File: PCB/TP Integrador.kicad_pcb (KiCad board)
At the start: 2 copper layers, 28 parts, among them Q1 BC547C, Q10 BC547C, Q2 2N3019, Q3 D45H11, Q4 BC547C, Q5 BC557C, Q6 BC557C, Q7 BC547C, Q8 BC557C, Q9 BC547C

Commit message: Upate PCB
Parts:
- added C1: C, Capacitor_THT:CP_Radial_D4.0mm_P1.50mm, F.Cu at (167.6, 86.4)
- added Q11: BC547C, Package_TO_SOT_THT:TO-92_Inline_Wide, F.Cu at (160.0, 73.7)
- added RL2: 50, Resistor_THT:R_Axial_DIN0207_L6.3mm_D2.5mm_P7.62mm_Horizontal, F.Cu at (165.1, 59.7)
- added RL3: 50, Resistor_THT:R_Axial_DIN0207_L6.3mm_D2.5mm_P5.08mm_Vertical, F.Cu at (163.0, 77.6)
- added RL4: 50, Resistor_THT:R_Axial_DIN0207_L6.3mm_D2.5mm_P5.08mm_Vertical, F.Cu at (167.6, 81.3)
- moved H3 2.54 mm to (165.1, 106.7)
- moved H4 2.54 mm to (165.1, 43.2)
- moved RD1 2.54 mm to (160.0, 83.8)
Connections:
- Q2 pad 3: vo -> Net-(Q2-E)
- Q3 pad 1: vo -> Net-(Q2-E)
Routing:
- net Net-(Q2-E): track 0.00 -> 41.1 mm
- net GND: track 17.7 -> 8.30 mm
- net Net-(Q11-B): track 0.00 -> 7.96 mm
- net Net-(JP1-B): track 13.5 -> 7.19 mm
- net Net-(Q11-C): track 36.5 -> 42.7 mm
- net vo: track 37.9 -> 31.8 mm

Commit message: Update checkpoint 2
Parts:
- removed C1: C, Capacitor_THT:CP_Radial_D4.0mm_P1.50mm
- removed Q7: BC547C, Package_TO_SOT_THT:TO-92_Inline_Wide
- removed Q8: BC557C, Package_TO_SOT_THT:TO-92_Inline_Wide
- removed RB1: 51, Resistor_THT:R_Axial_DIN0207_L6.3mm_D2.5mm_P7.62mm_Horizontal
- removed RB2: 1.8k, Resistor_THT:R_Axial_DIN0207_L6.3mm_D2.5mm_P7.62mm_Horizontal
- removed RL2: 50, Resistor_THT:R_Axial_DIN0207_L6.3mm_D2.5mm_P7.62mm_Horizontal
- removed RL3, RL4: 50, Resistor_THT:R_Axial_DIN0207_L6.3mm_D2.5mm_P5.08mm_Vertical
- removed VREF1: 1.56, TerminalBlock_Phoenix:TerminalBlock_Phoenix_MKDS-1,5-2-5.08_1x02_P5.08mm_Horizontal
- added CComp1: 12n, Capacitor_THT:CP_Radial_D4.0mm_P1.50mm, F.Cu at (145.2, 74.2)
- added CL1: 2.2u, Capacitor_THT:CP_Radial_D4.0mm_P1.50mm, F.Cu at (183.5, 72.3)
- added JP3: Jumper_2_Bridged, TestPoint:TestPoint_2Pads_Pitch5.08mm_Drill1.3mm, F.Cu at (159.1, 51.4)
- added JP4: Jumper_2_Bridged, TestPoint:TestPoint_2Pads_Pitch5.08mm_Drill1.3mm, F.Cu at (189.5, 53.6)
- added R8: 2200, Resistor_THT:R_Axial_DIN0207_L6.3mm_D2.5mm_P7.62mm_Horizontal, F.Cu at (91.8, 58.2)
- added RP1: 50, Resistor_THT:R_Axial_DIN0207_L6.3mm_D2.5mm_P5.08mm_Vertical, F.Cu at (164.2, 60.3)
- added RP2: 50, Resistor_THT:R_Axial_DIN0207_L6.3mm_D2.5mm_P5.08mm_Vertical, F.Cu at (164.2, 69.1)
- added RS1: 2.2, Resistor_THT:R_Axial_DIN0207_L6.3mm_D2.5mm_P7.62mm_Horizontal, F.Cu at (168.4, 51.6)
- added U1: TL431D, Package_TO_SOT_THT:TO-92_Inline_Wide, F.Cu at (92.3, 75.4)
- Q2: value 2N3019 -> 2SB631; footprint Package_TO_SOT_THT:TO-39-3 -> Package_TO_SOT_THT:TO-126-3_Vertical
- Q3: value D45H11 -> BC547; footprint Package_TO_SOT_THT:TO-220-3_Vertical -> Package_TO_SOT_THT:TO-92_Inline_Wide
- RD1: value 2.2k -> 1k
- moved H3 67.1 mm to (188.2, 43.7)
- moved H2 64.5 mm to (80.1, 42.5)
- moved H4 59.7 mm to (190.1, 97.3)
- moved H1 53.4 mm to (81.6, 96.3)
- moved RL1 33.1 mm to (189.4, 72.4)
- moved JP2 26.8 mm to (135.4, 51.1)
- moved Q9 26.6 mm to (129.1, 86.5)
- moved Q10 21.1 mm to (109.9, 86.2)
- moved JP1 20.4 mm to (158.8, 79.4)
- moved RD1 19.7 mm to (175.7, 71.9), turned to -90 degrees
- moved RD2 17.0 mm to (168.9, 83.5), turned to 180 degrees
- moved Q11 16.8 mm to (175.4, 66.8), turned to 90 degrees
- moved Q3 16.0 mm to (146.3, 62.2), turned to 0 degrees
- moved R2 14.8 mm to (103.3, 91.2), turned to 180 degrees
- moved RE1 14.5 mm to (122.0, 91.3), turned to -90 degrees
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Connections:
- net vref renamed Net-(Q1-B)
- JP2 pad 1: Net-(JP2-A) -> vi
- Q1 pad 1: Net-(JP2-A) -> Net-(Q1-C)
- Q11 pad 3: vo -> Net-(JP4-A)
- Q2 pad 1: Net-(Q2-C) -> Net-(JP2-B)
- Q2 pad 2: Net-(Q11-C) -> Net-(JP3-A)
- Q3 pad 2: Net-(Q2-C) -> Net-(Q11-C)
- Q3 pad 3: vi -> Net-(JP3-A)
- Q4 pad 1: Net-(Q4-C) -> Net-(Q11-C)
- Q5 pad 1: Net-(Q4-C) -> Net-(Q11-C)
- Q5 pad 2: Net-(Q4-C) -> Net-(Q1-C)
- Q6 pad 1: Net-(JP2-A) -> Net-(Q1-C)
- Q6 pad 2: Net-(Q4-C) -> Net-(Q1-C)
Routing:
- net GND: track 8.30 -> 212.7 mm
- net Net-(Q4-C): track 50.0 -> 0.00 mm
- net Net-(Q10-B): track 64.2 -> 26.1 mm
- net Net-(Q1-C): track 0.00 -> 37.5 mm
- net Net-(Q2-B): track 41.1 -> 5.98 mm
- net Net-(JP2-A): track 32.2 -> 0.00 mm
- net Net-(Q11-C): track 42.7 -> 74.4 mm
- net Net-(JP4-A): track 0.00 -> 24.7 mm
- net Net-(JP3-A): track 0.00 -> 21.3 mm
- net Net-(JP1-A): track 13.5 -> 29.9 mm
- net Net-(Q8-E): track 15.6 -> 0.00 mm
- net Net-(Q2-C): track 13.8 -> 0.00 mm
- net Net-(JP3-B): track 0.00 -> 8.26 mm
- net Net-(JP1-B): track 7.19 -> 15.2 mm
- net Net-(Q11-B): track 7.96 -> 14.9 mm
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- removed copper zone on B.Cu, net GND

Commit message: Edit Checkpoint 2
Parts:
- added JP5: Jumper_2_Bridged, TestPoint:TestPoint_2Pads_Pitch5.08mm_Drill1.3mm, F.Cu at (117.7, 82.0)
- added JP6: Jumper_2_Bridged, TestPoint:TestPoint_2Pads_Pitch5.08mm_Drill1.3mm, F.Cu at (134.4, 73.5)
- added JP7: Jumper_2_Bridged, TestPoint:TestPoint_2Pads_Pitch5.08mm_Drill1.3mm, F.Cu at (170.6, 63.6)
- added JP8: Jumper_2_Bridged, TestPoint:TestPoint_2Pads_Pitch5.08mm_Drill1.3mm, F.Cu at (93.6, 75.8)
- CComp1, CL1: footprint Capacitor_THT:CP_Radial_D4.0mm_P1.50mm -> Capacitor_THT:CP_Radial_D8.0mm_P3.80mm
- moved Q11 7.13 mm to (182.5, 66.3)
- moved CL1 5.07 mm to (180.9, 76.6)
- moved U1 3.96 mm to (88.3, 75.4)
- moved VI1 3.76 mm to (83.7, 50.8)
- moved H2 3.56 mm to (83.6, 42.5)
- moved RD1 3.37 mm to (172.4, 72.2)
- moved H1 2.30 mm to (83.6, 97.4)
- moved H4 1.52 mm to (188.6, 97.4)
- moved H3 1.33 mm to (188.6, 42.5)
- moved CComp1 1.17 mm to (144.4, 73.3), turned to 0 degrees
- moved Q2 0.11 mm to (146.6, 51.2)
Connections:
- CComp1 pad 1: Net-(Q11-C) -> Net-(JP6-B)
- Q1 pad 2: Net-(Q1-B) -> Net-(JP8-B)
- Q1 pad 3: Net-(Q1-E) -> Net-(JP5-A)
- Q11 pad 1: Net-(Q11-C) -> Net-(JP6-B)
- Q11 pad 2: Net-(Q11-B) -> Net-(JP7-B)
- Q3 pad 2: Net-(Q11-C) -> Net-(JP6-B)
- Q4 pad 1: Net-(Q11-C) -> Net-(JP6-A)
- Q4 pad 3: Net-(Q1-E) -> Net-(JP5-B)
- Q5 pad 1: Net-(Q11-C) -> Net-(JP6-A)
- Q9 pad 1: Net-(Q1-E) -> Net-(JP5-A)
- R1 pad 1: Net-(Q1-B) -> Net-(JP8-B)
- R8 pad 2: Net-(Q1-B) -> Net-(JP8-A)
- RP1 pad 1: Net-(Q11-B) -> Net-(JP7-A)
- RP2 pad 2: Net-(Q11-B) -> Net-(JP7-A)
- U1 pad 1: Net-(Q1-B) -> Net-(JP8-A)
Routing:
- net Net-(Q11-C): track 74.4 -> 0.00 mm
- net Net-(JP6-B): track 0.00 -> 52.8 mm
- net Net-(Q1-E): track 32.2 -> 0.00 mm
- net Net-(JP5-A): track 0.00 -> 30.0 mm
- net Net-(Q1-B): track 27.9 -> 0.00 mm
- net Net-(JP8-A): track 0.00 -> 16.2 mm
- net Net-(JP6-A): track 0.00 -> 15.5 mm
- net Net-(Q11-B): track 14.9 -> 0.00 mm
- net Net-(JP8-B): track 0.00 -> 14.9 mm
- net GND: track 212.7 -> 202.2 mm
- net Net-(JP7-A): track 0.00 -> 10.3 mm
- net vo: track 27.6 -> 37.0 mm
- net Net-(JP7-B): track 0.00 -> 6.84 mm
- net Net-(JP5-B): track 0.00 -> 6.12 mm
- net vi: track 70.5 -> 66.7 mm
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
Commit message: Falta el disipador!!!
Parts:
- CL1: value 2.2u -> Jumper_2_Bridged; footprint Capacitor_THT:CP_Radial_D8.0mm_P3.80mm -> TestPoint:TestPoint_2Pads_Pitch5.08mm_Drill1.3mm
- RL1: value 50 -> Jumper_2_Bridged; footprint Resistor_THT:R_Axial_DIN0207_L6.3mm_D2.5mm_P7.62mm_Horizontal -> TestPoint:TestPoint_2Pads_Pitch5.08mm_Drill1.3mm
- moved CL1 2.05 mm to (181.2, 74.6)
- moved RL1 0.94 mm to (190.1, 73.0)
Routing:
- net GND: track 202.2 -> 210.1 mm
- net vo: track 37.0 -> 34.1 mm

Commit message: Edit Rs, no falta el disipador!!
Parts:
- added J1: Conn_01x01_Pin, Connector_PinHeader_1.00mm:PinHeader_1x01_P1.00mm_Vertical, F.Cu at (101.7, 72.2)
- added J2: Conn_01x01_Pin, Connector_PinHeader_1.00mm:PinHeader_1x01_P1.00mm_Vertical, F.Cu at (128.8, 72.8)
- RS1: footprint Resistor_THT:R_Axial_DIN0207_L6.3mm_D2.5mm_P7.62mm_Horizontal -> Resistor_THT:R_Axial_DIN0617_L17.0mm_D6.0mm_P20.32mm_Horizontal
- moved RS1 11.1 mm to (161.5, 42.9)
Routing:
- net Net-(JP3-B): track 8.55 -> 13.8 mm

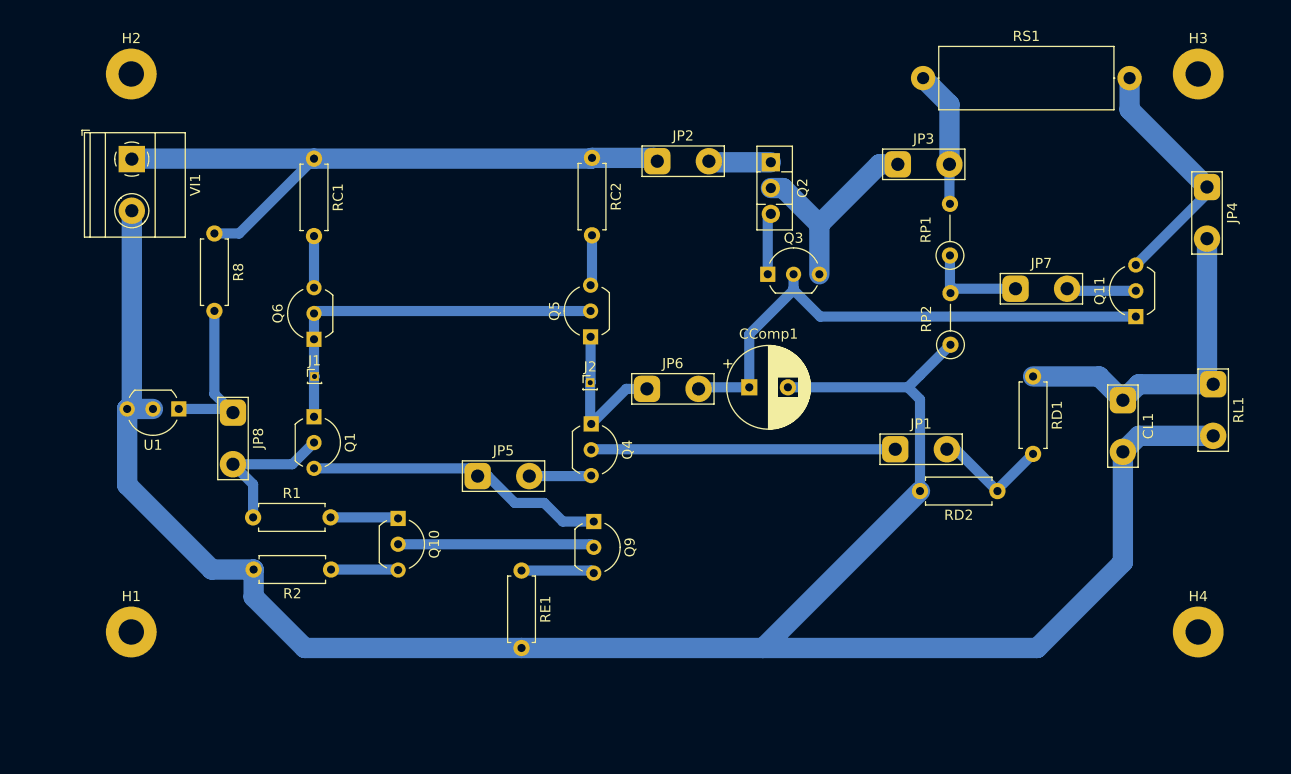
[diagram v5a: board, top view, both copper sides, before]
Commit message: Edit pads para que sean mas gorditos
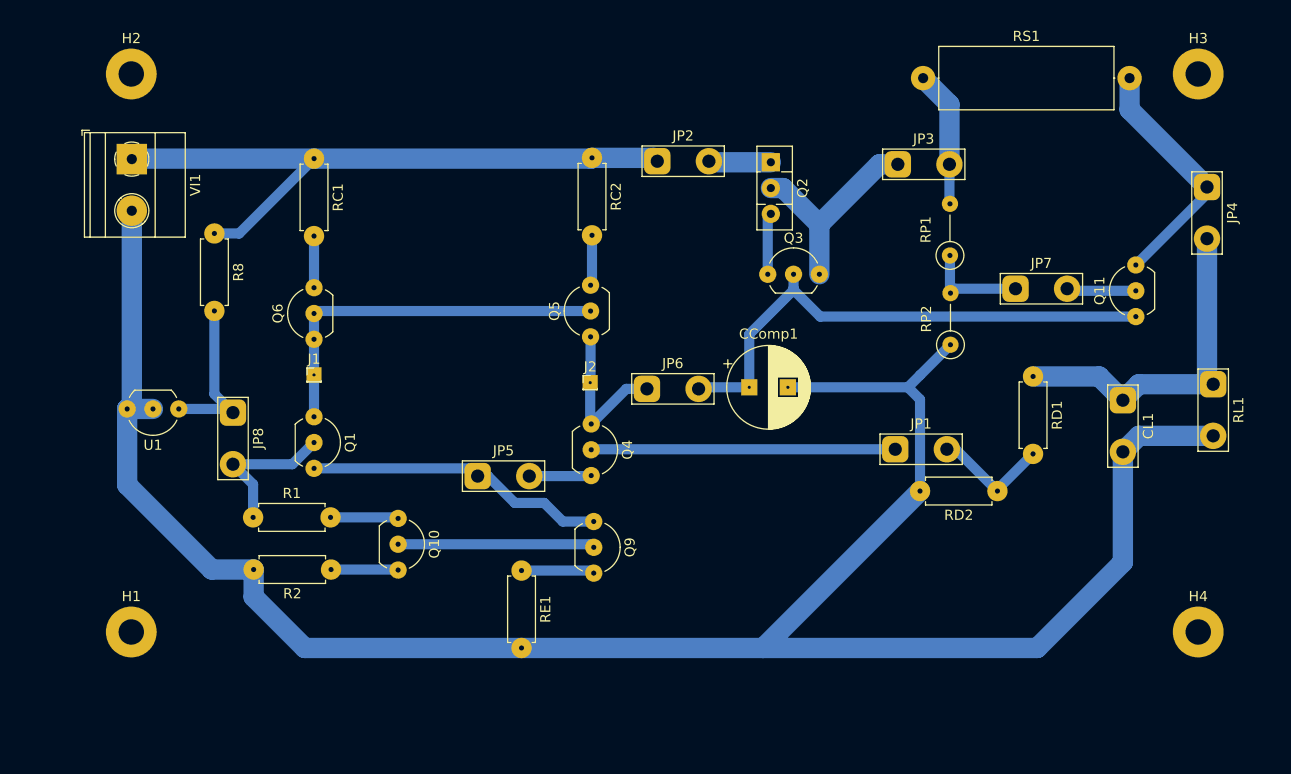
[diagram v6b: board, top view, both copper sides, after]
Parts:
- moved J1 0.16 mm to (101.6, 72.1)
